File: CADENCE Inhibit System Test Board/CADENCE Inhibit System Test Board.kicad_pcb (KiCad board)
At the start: 2 copper layers, 70 x 72.5 mm, 65 parts, among them IC1 LTC7004IMSE#WTRPBF, IC2 LTC7004IMSE#WTRPBF, IC3 LTC7004IMSE#WTRPBF, IC4 LTC7004IMSE#WTRPBF, IC5 LTC7004IMSE#WTRPBF, J1 INHIBIT_P2, J10 Conn_01x04, J11 Conn_01x02, J2 INHIBIT_P2, J3 INHIBIT_P2, J4 INHIBIT_P2, J5 INHIBIT_P2, J6 INHIBIT_P2, J7 INHIBIT_P2, J8 INHIBIT_P2, J9 INHIBIT_P2, Q1 SUD23N06-31-GE3, Q2 SUD23N06-31-GE3, Q3 SUD23N06-31-GE3, Q4 SUD23N06-31-GE3, Q5 SUD23N06-31-GE3, Q6 SUD23N06-31-GE3, Q7 SUD23N06-31-GE3, U1 MIC4427YM-TR, U2 MIC4427YM-TR

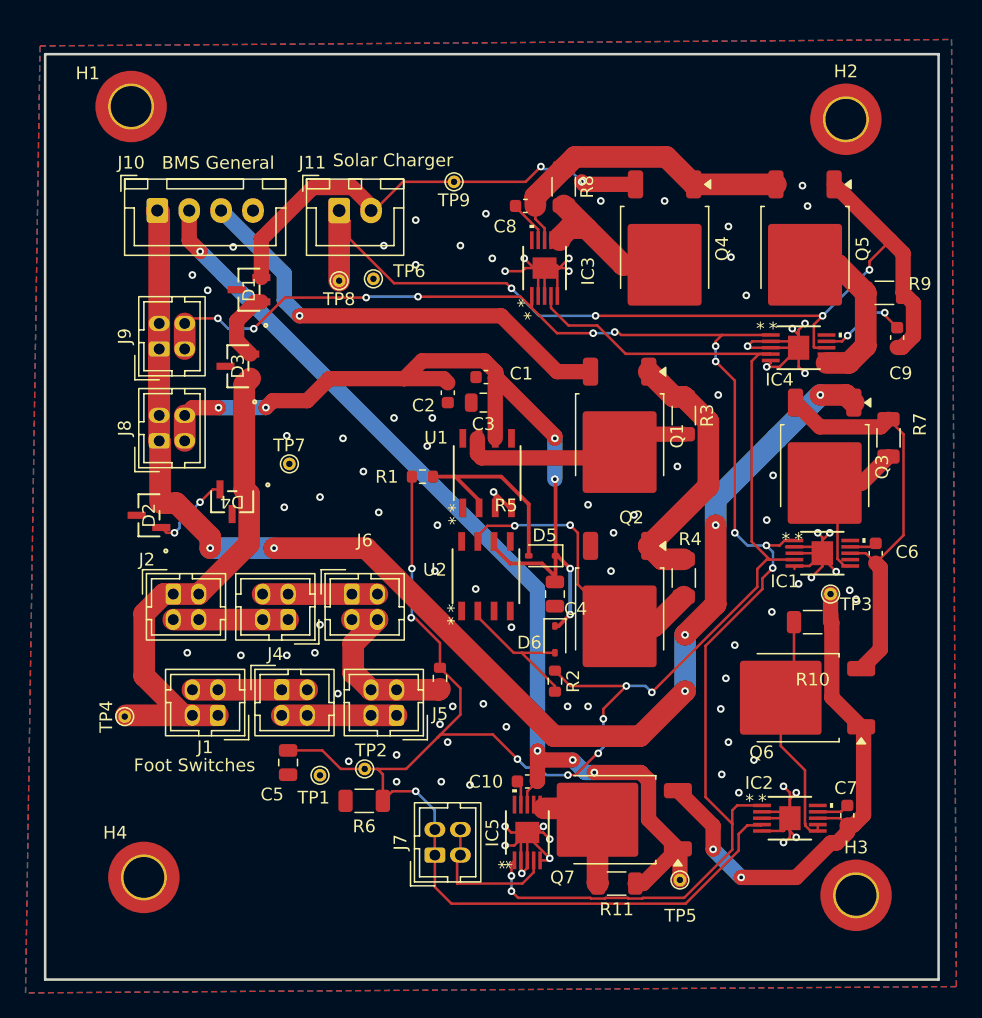
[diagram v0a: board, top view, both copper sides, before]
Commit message: rearranged testpoints
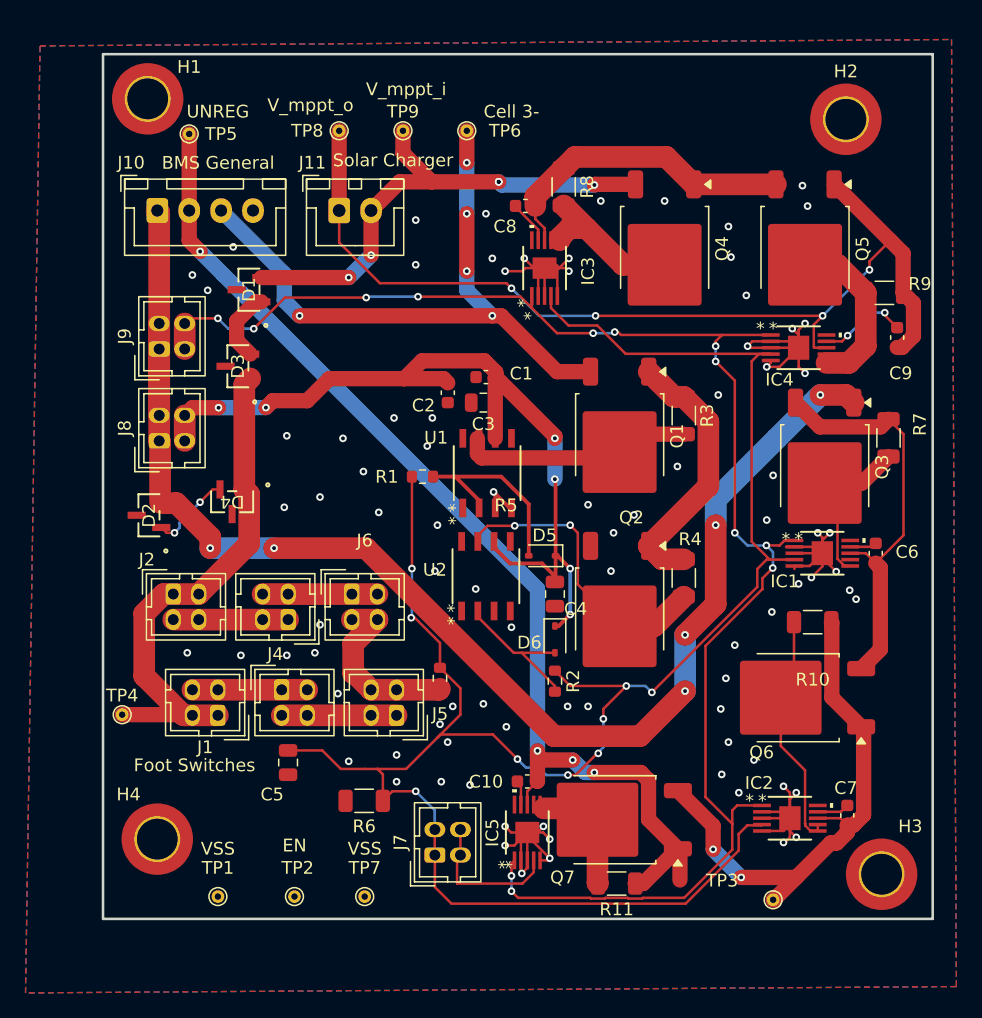
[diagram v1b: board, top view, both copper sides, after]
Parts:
- moved TP5 70.0 mm to (131.8, 44.8)
- moved TP7 34.4 mm to (145.5, 104.5)
- moved TP3 24.4 mm to (177.5, 104.8)
- moved TP6 13.7 mm to (153.5, 44.5)
- moved TP1 12.4 mm to (134.0, 104.5)
- moved TP8 11.8 mm to (143.5, 44.5)
- moved TP2 11.4 mm to (140.0, 104.5)
- moved TP9 5.66 mm to (148.5, 44.5)
- moved H4 3.18 mm to (129.2, 100.0)
- moved H3 2.59 mm to (186.0, 102.8)
- moved H1 1.43 mm to (128.5, 42.0)
- moved TP4 0.25 mm to (126.5, 90.2)
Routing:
- net Cell 3-: track 35.4 -> 50.7 mm, vias 1 -> 5
- net UNREG: track 80.9 -> 86.9 mm
- net V_mppt_i: track 37.0 -> 39.5 mm, vias 2 -> 5
- net V_mppt_o: track 75.6 -> 77.0 mm
- net VSS: vias 90 -> 88
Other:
- board size 70 x 72.5 mm -> 65 x 67.8 mm

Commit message: compression and decor
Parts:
- added G***: LOGO, LOGO, F.Cu at (170.5, 44.5)
- added G***: LOGO, LOGO, F.Cu at (159.0, 93.5)
- added G***: LOGO, LOGO, F.Cu at (177.0, 44.5)
- added G***: LOGO, LOGO, F.Cu at (152.0, 52.0)
- added G***: LOGO, LOGO, F.Cu at (168.5, 92.5)
- added G***: LOGO, LOGO, F.Cu at (178.0, 92.0)
- added G***: LOGO, LOGO, F.Cu at (174.5, 55.5)
- added G***: LOGO, LOGO, F.Cu at (135.5, 68.0)
- added G***: LOGO, LOGO, B.Cu at (179.5, 87.0)
- moved R11 39.7 mm to (161.0, 64.0), turned to -90 degrees
- moved IC2 31.5 mm to (186.0, 67.7), turned to -90 degrees
- moved C10 31.0 mm to (159.0, 64.5), turned to -90 degrees
- moved IC5 28.5 mm to (160.0, 71.0)
- moved TP3 25.5 mm to (185.5, 80.5)
- moved C7 20.8 mm to (185.5, 77.5), turned to 0 degrees
- moved J7 20.6 mm to (157.0, 81.5)
- moved C5 19.8 mm to (158.0, 87.0), turned to -90 degrees
- moved D5 19.6 mm to (144.5, 65.0)
- moved R6 18.2 mm to (161.0, 87.5), turned to 90 degrees
- moved R4 17.0 mm to (171.0, 62.5), turned to 180 degrees
- moved Q7 16.3 mm to (167.0, 82.3), turned to 90 degrees
- moved TP2 15.2 mm to (151.0, 94.0)
- moved C3 15.1 mm to (140.0, 63.0)
- moved Q1 14.1 mm to (152.3, 63.5)
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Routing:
- net EN: track 162.7 -> 113.6 mm, vias 9 -> 5
- net LOW_SIDE_PWR: track 68.6 -> 45.2 mm, vias 6 -> 2
- net VSS: track 86.1 -> 109.0 mm, vias 88 -> 79
- net Cell 1+: track 111.2 -> 89.7 mm, vias 6 -> 2
- net HIGH_SIDE_PWR: track 125.7 -> 106.4 mm, vias 13 -> 9
- net Cell 3-: track 50.7 -> 35.0 mm, vias 5 -> 0
- net Net-(IC5-TGDN): track 9.59 -> 19.5 mm
- net UNREG: track 86.9 -> 77.3 mm, vias 4 -> 7
- net V_mppt_i: track 39.5 -> 48.9 mm, vias 5 -> 3
- net Net-(IC2-TS): track 42.0 -> 33.5 mm, vias 2 -> 0
- net Net-(IC1-TS): track 33.2 -> 26.7 mm
- net Net-(IC2-BST): track 2.52 -> 7.72 mm
- net Net-(Q1-G): track 18.3 -> 23.3 mm
- net Net-(J5-Pin_2): track 14.4 -> 19.1 mm
- net Net-(D3-K): track 41.2 -> 45.2 mm
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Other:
- board size 65 x 67.8 mm -> 65 x 58 mm

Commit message: minor capacitor movement
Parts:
- moved C7 5.39 mm to (187.5, 72.5)
- moved TP3 4.92 mm to (187.5, 76.0)
- moved C9 3.73 mm to (183.5, 61.0)
- moved R9 3.38 mm to (185.5, 60.5), turned to -90 degrees
- moved C10 1.58 mm to (158.5, 66.0)
- moved R11 1.58 mm to (160.5, 65.5), turned to 90 degrees
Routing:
- net Net-(Q2-G): track 27.0 -> 40.0 mm
- net V_mppt_o: track 74.8 -> 63.9 mm, vias 4 -> 2
- net Net-(IC4-BST): track 7.07 -> 2.14 mm, vias 2 -> 0
- net Net-(IC2-BST): track 7.72 -> 3.37 mm
- net UNREG: track 77.3 -> 79.9 mm, vias 7 -> 6
- net Net-(IC5-TGDN): track 19.5 -> 21.3 mm
- net Net-(IC5-BST): track 3.75 -> 2.45 mm
- net Net-(IC2-TS): track 33.5 -> 32.5 mm
- net VSS: vias 79 -> 78

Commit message: label change and pos and bom stuff
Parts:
- renumbered TP3 to GSE
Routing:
- net VSS: vias 78 -> 76

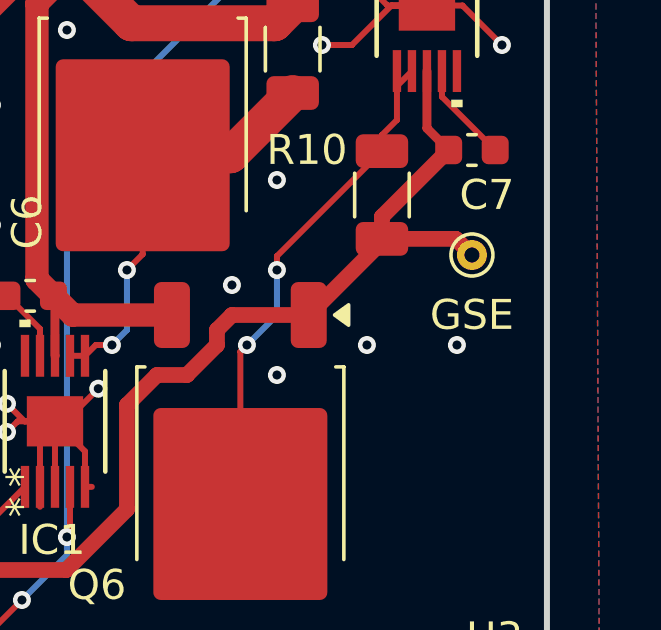
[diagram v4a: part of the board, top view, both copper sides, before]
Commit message: changed placement of gse via
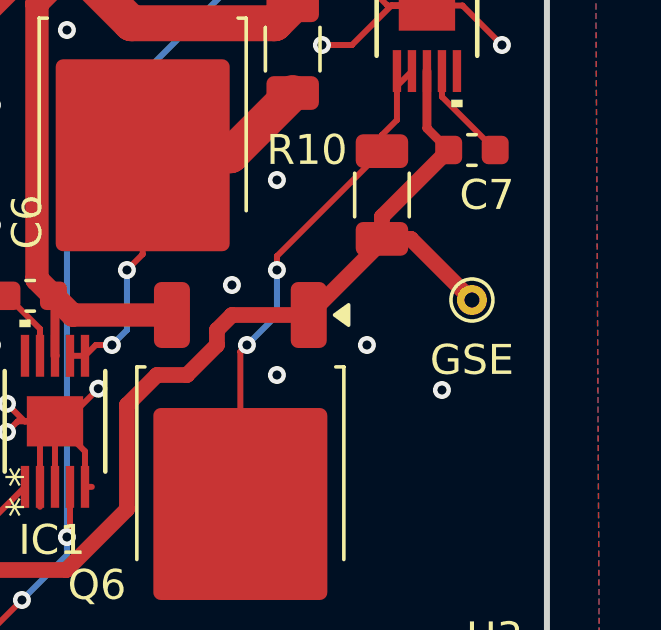
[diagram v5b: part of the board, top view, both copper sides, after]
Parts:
- moved GSE 1.50 mm to (187.5, 77.5)
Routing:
- net Net-(IC2-TS): track 32.5 -> 33.2 mm
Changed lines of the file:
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@@
 	(footprint "TestPoint:TestPoint_THTPad_D1.0mm_Drill0.5mm"
 		(layer "F.Cu")
-		(at 187.5 76)
+		(at 187.5 77.5)
 		(descr "THT pad as test Point, diameter 1.0mm, hole diameter 0.5mm")
 		(tags "test point THT pad")
@@
 	)
 	(via
-		(at 187 79)
+		(at 186.5 80.5)
 		(size 0.6)
 		(drill 0.3)
@@
 	)
 	(segment
-		(start 184.5 74.725)
-		(end 186.725 72.5)
+		(start 184.5 75.4625)
+		(end 185.4625 75.4625)
 		(width 0.526)
 		(layer "F.Cu")
@@
 	)
 	(segment
-		(start 170.08 86.5)
-		(end 169.28 87.3)
+		(start 184.5 74.725)
+		(end 186.725 72.5)
 		(width 0.526)
 		(layer "F.Cu")
@@
 	)
 	(segment
-		(start 179.5 78)
-		(end 179 78.5)
+		(start 170.08 86.5)
+		(end 169.28 87.3)
 		(width 0.526)
 		(layer "F.Cu")
@@
 	)
 	(segment
-		(start 176 84.479045)
-		(end 173.979045 86.5)
+		(start 185.4625 75.4625)
+		(end 187.5 77.5)
 		(width 0.526)
 		(layer "F.Cu")
@@
 	)
 	(segment
-		(start 186.9625 75.4625)
-		(end 187.5 76)
+		(start 179.5 78)
+		(end 179 78.5)
 		(width 0.526)
 		(layer "F.Cu")
@@
 	)
 	(segment
-		(start 184.5 75.4625)
-		(end 184.5 75.56)
+		(start 176 84.479045)
+		(end 173.979045 86.5)
 		(width 0.526)
 		(layer "F.Cu")
@@
 	(segment
 		(start 184.5 75.4625)
-		(end 186.9625 75.4625)
+		(end 184.5 75.56)
 		(width 0.526)
 		(layer "F.Cu")

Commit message: fixed diode footprints and added gbr and drl files
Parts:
- moved D4 1.00 mm to (132.8, 74.6), turned to -90 degrees
- moved D3 0.60 mm to (135.4, 61.6), turned to 180 degrees
- moved D2 0.53 mm to (128.4, 73.6), turned to -90 degrees
- turned D1 to 180 degrees
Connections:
- D1 pad 1: Net-(D1-K) -> V_mppt_i
- D1 pad 2: V_mppt_i -> (no net)
- D1 pad 3: (no net) -> Net-(D1-K)
- D2 pad 1: Net-(D2-K) -> Cell 1+
- D2 pad 2: Cell 1+ -> (no net)
- D2 pad 3: (no net) -> Net-(D2-K)
- D3 pad 1: Net-(D3-K) -> Net-(D1-K)
- D3 pad 2: Net-(D1-K) -> (no net)
- D3 pad 3: (no net) -> Net-(D3-K)
- D4 pad 1: Net-(D3-K) -> Net-(D2-K)
- D4 pad 2: Net-(D2-K) -> (no net)
- D4 pad 3: (no net) -> Net-(D3-K)
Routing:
- net V_mppt_i: track 48.9 -> 46.6 mm
- net Cell 1+: track 89.7 -> 87.6 mm
- net Net-(D1-K): track 4.11 -> 2.70 mm
- net Net-(D2-K): track 3.75 -> 2.40 mm
- net Net-(D3-K): track 45.2 -> 46.5 mm
- net VSS: vias 76 -> 75
- net UNREG: vias 6 -> 5
